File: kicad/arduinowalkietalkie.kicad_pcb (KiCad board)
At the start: 2 copper layers, 112 x 100 mm, 32 parts, among them SW1 SW_Push_Dual, SW10 SW_Push_Dual, SW11 SW_Push_Dual, SW12 SW_Push_Dual, SW13 SW_Push_Dual, SW14 SW_Push_Dual, SW2 SW_Push_Dual, SW3 SW_Push_Dual, SW4 SW_Push_Dual, SW5 SW_Push_Dual, SW6 SW_Push_Dual, SW7 SW_Push_Dual, SW8 SW_Push_Dual, SW9 SW_Push_Dual, U1 NRF24L01_Breakout

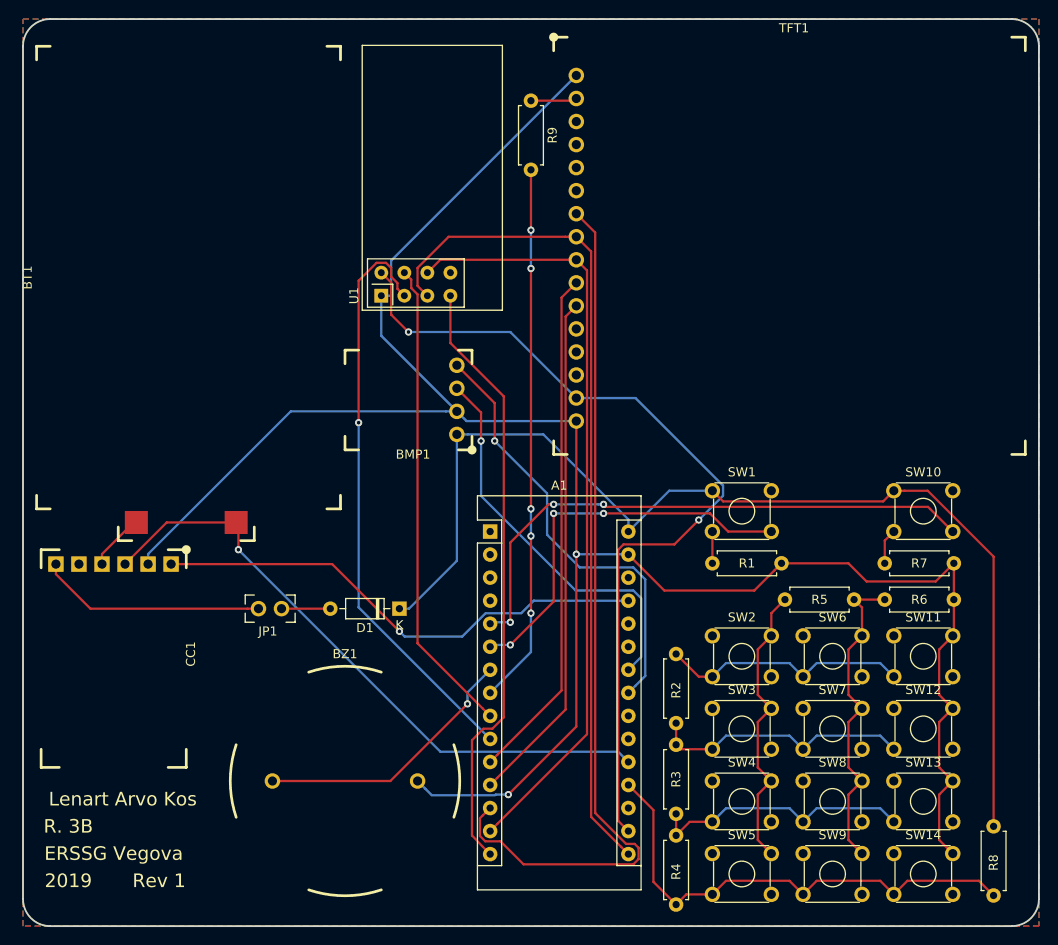
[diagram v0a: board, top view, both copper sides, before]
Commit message: compacted pcb to 100mmx100mm
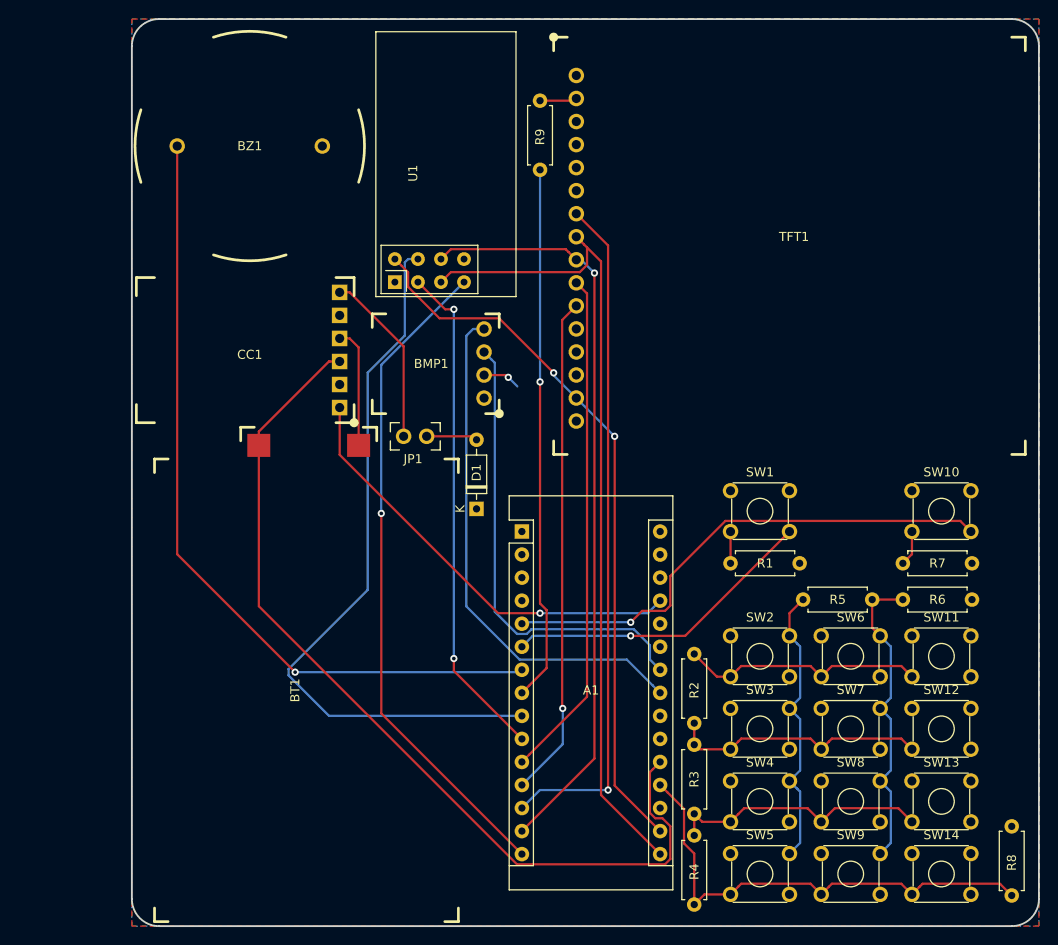
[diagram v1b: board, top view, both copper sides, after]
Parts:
- moved BZ1 70.8 mm to (111.0, 54.0)
- moved BT1 46.7 mm to (116.0, 114.0), turned to 270 degrees
- moved CC1 36.0 mm to (111.0, 77.0), turned to 180 degrees
- moved JP1 24.8 mm to (129.0, 86.0)
- moved D1 13.9 mm to (136.0, 94.0), turned to 90 degrees
- moved BMP1 5.00 mm to (131.0, 78.0)
- moved A1 3.50 mm to (141.0, 96.5)
- moved U1 2.12 mm to (127.0, 69.0)
- moved R1 2.00 mm to (164.0, 100.0)
- moved R2 2.00 mm to (160.0, 110.0)
- moved R3 2.00 mm to (160.0, 120.0)
- moved R4 2.00 mm to (160.0, 130.0)
- moved R5 2.00 mm to (179.6, 104.0)
- moved R6 2.00 mm to (190.6, 100.0)
- moved R7 2.00 mm to (183.0, 104.0)
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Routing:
- net GND: track 242.2 -> 4.19 mm, vias 2 -> 1
- net +5V: track 122.4 -> 0.00 mm
- net Net-(A1-Pad7): track 29.8 -> 88.5 mm
- net Net-(A1-Pad20): track 69.9 -> 101.3 mm, vias 1 -> 0
- net Net-(A1-Pad9): track 52.8 -> 80.0 mm
- net Net-(A1-Pad13): track 97.1 -> 75.3 mm, vias 0 -> 1
- net Net-(A1-Pad17): track 96.1 -> 79.0 mm
- net Net-(A1-Pad10): track 64.8 -> 55.7 mm, vias 1 -> 2
- net Net-(A1-Pad6): track 43.6 -> 34.8 mm, vias 3 -> 1
- net SDA: track 48.9 -> 57.4 mm, vias 1 -> 0
- net SCL: track 43.8 -> 51.3 mm, vias 1 -> 0
- net Net-(A1-Pad27): track 55.4 -> 48.3 mm
- net Net-(BT1-Pad2): track 6.34 -> 13.3 mm
- net MISO: track 66.8 -> 73.3 mm, vias 0 -> 1
- net Net-(A1-Pad5): track 62.8 -> 56.6 mm, vias 3 -> 1
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- added copper zone on F.Cu, net +5V
- added copper zone on B.Cu, net GND
- removed copper zone on B.Cu, net +5V
- removed copper zone on F.Cu, net GND
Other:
- board size 112 x 100 mm -> 100 x 100 mm
- board text added: "Rev 1.1"
- board text removed: "Rev 1"

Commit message: update pcb
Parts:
- added JP2: Jumper, PIN_JUMPER:PIN_JUMPER, F.Cu at (118.0, 86.0)
- added R10: 2k7, Resistor_THT:R_Axial_DIN0207_L6.3mm_D2.5mm_P7.62mm_Horizontal, B.Cu at (152.5, 59.5)
- added R11: 2k7, Resistor_THT:R_Axial_DIN0207_L6.3mm_D2.5mm_P7.62mm_Horizontal, B.Cu at (152.5, 63.0)
- added R12: 2k7, Resistor_THT:R_Axial_DIN0207_L6.3mm_D2.5mm_P7.62mm_Horizontal, B.Cu at (152.5, 66.5)
- added R13: 2k7, Resistor_THT:R_Axial_DIN0207_L6.3mm_D2.5mm_P7.62mm_Horizontal, B.Cu at (152.5, 70.0)
- added R14: 2k7, Resistor_THT:R_Axial_DIN0207_L6.3mm_D2.5mm_P7.62mm_Horizontal, B.Cu at (152.5, 73.5)
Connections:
- CC1 pad 1: Net-(A1-Pad27) -> Net-(CC1-Pad1)
- TFT1 pad 10: Net-(A1-Pad11) -> Net-(R13-Pad1)
- TFT1 pad 11: Net-(A1-Pad12) -> Net-(R14-Pad1)
- TFT1 pad 7: Net-(A1-Pad13) -> Net-(R10-Pad1)
- TFT1 pad 8: SCK -> Net-(R11-Pad1)
- TFT1 pad 9: MOSI -> Net-(R12-Pad1)
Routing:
- net MOSI: track 83.3 -> 108.7 mm, vias 1 -> 0
- net SCK: track 90.7 -> 106.6 mm, vias 0 -> 1
- net Net-(A1-Pad13): track 75.3 -> 83.0 mm
- net Net-(R10-Pad1): track 0.00 -> 6.31 mm
- net Net-(R14-Pad1): track 0.00 -> 6.28 mm
- net Net-(R11-Pad1): track 0.00 -> 5.91 mm
- net Net-(R13-Pad1): track 0.00 -> 5.88 mm
- net Net-(CC1-Pad1): track 0.00 -> 5.72 mm
- net Net-(R12-Pad1): track 0.00 -> 5.52 mm
- net Net-(A1-Pad11): track 56.3 -> 61.3 mm
- net Net-(A1-Pad12): track 55.4 -> 58.9 mm
- net Net-(A1-Pad27): track 48.3 -> 45.9 mm
- net GND: track 4.19 -> 2.77 mm

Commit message: New pcb
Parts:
- added C1: C, Capacitor_THT:C_Disc_D4.7mm_W2.5mm_P5.00mm, F.Cu at (145.5, 90.0)
- added C2: C, Capacitor_THT:C_Disc_D4.7mm_W2.5mm_P5.00mm, F.Cu at (179.5, 92.0)
- added C3: C, Capacitor_THT:C_Disc_D4.7mm_W2.5mm_P5.00mm, F.Cu at (106.6, 86.7)
- added C4: C, Capacitor_THT:C_Disc_D4.7mm_W2.5mm_P5.00mm, F.Cu at (142.5, 68.5)
- added R15: 220, Resistor_THT:R_Axial_DIN0207_L6.3mm_D2.5mm_P7.62mm_Horizontal, F.Cu at (102.0, 80.0)
- added R16: 10K, Resistor_THT:R_Axial_DIN0207_L6.3mm_D2.5mm_P7.62mm_Horizontal, F.Cu at (136.5, 130.0)
- R10, R11, R12, R13, R14: moved to F.Cu
- moved R10 22.1 mm to (172.0, 70.0)
- moved R11 22.1 mm to (172.0, 73.5)
- moved R12 22.1 mm to (172.0, 77.0)
- moved R13 22.1 mm to (172.0, 80.5)
- moved R14 22.1 mm to (172.0, 84.0)
- moved JP2 2.08 mm to (116.0, 86.6)
- moved BT1 1.45 mm to (114.7, 113.4)
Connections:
- A1 pad 27: Net-(A1-Pad27) -> +5V
- A1 pad 30: +5V -> Net-(A1-Pad30)
- BT1 pad 1: Net-(A1-Pad20) -> Net-(BT1-Pad1)
- BZ1 pad 1: Net-(A1-Pad7) -> Net-(BZ1-Pad1)
- CC1 pad 3: Net-(A1-Pad20) -> Net-(BT1-Pad1)
- JP2 pad 1: Net-(A1-Pad27) -> +5V
- R11 pad 2: SCK -> Net-(A1-Pad21)
- R12 pad 2: MOSI -> Net-(A1-Pad22)
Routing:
- net GND: track 2.77 -> 227.6 mm, vias 1 -> 0
- net +5V: track 0.00 -> 173.3 mm
- net Net-(A1-Pad20): track 101.3 -> 26.3 mm
- net Net-(BT1-Pad1): track 0.00 -> 74.6 mm
- net Net-(A1-Pad21): track 0.00 -> 56.6 mm
- net Net-(A1-Pad22): track 0.00 -> 49.5 mm
- net Net-(A1-Pad27): track 45.9 -> 0.00 mm, vias 1 -> 0
- net MOSI: track 108.7 -> 67.2 mm
- net Net-(A1-Pad7): track 88.5 -> 53.3 mm, vias 1 -> 0
- net Net-(R14-Pad1): track 6.28 -> 30.1 mm
- net Net-(R13-Pad1): track 5.88 -> 29.7 mm
- net Net-(R12-Pad1): track 5.52 -> 29.3 mm
- net Net-(R11-Pad1): track 5.91 -> 28.9 mm
- net SCK: track 106.6 -> 83.9 mm, vias 1 -> 0
- net Net-(R10-Pad1): track 6.31 -> 28.5 mm
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- removed copper zone on F.Cu, net +5V
- removed copper zone on B.Cu, net GND
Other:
- board text removed: "2019"
- board text removed: "ERSSG Vegova"
- board text removed: "Lenart Arvo Kos"
- board text removed: "R. 3B"
- board text removed: "Rev 1.1"
